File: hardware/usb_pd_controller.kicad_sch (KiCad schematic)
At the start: 85 parts, among them J4 DG142R-5.08-02P-14-00AH, J5 108-0902-001, J6 108-0903-001, Q1 BSS138, Q2 BSS138, Q3 SQJB60EP, Q5 SQJB60EP, U1 AP33772SDKZ-13-FA02, U11 TPS55340PWPR, U12 LM74801-Q1, U13 74LVC1G08, U3 INA226, U5 AOZ1284PI, U6 TL431AIDBZR

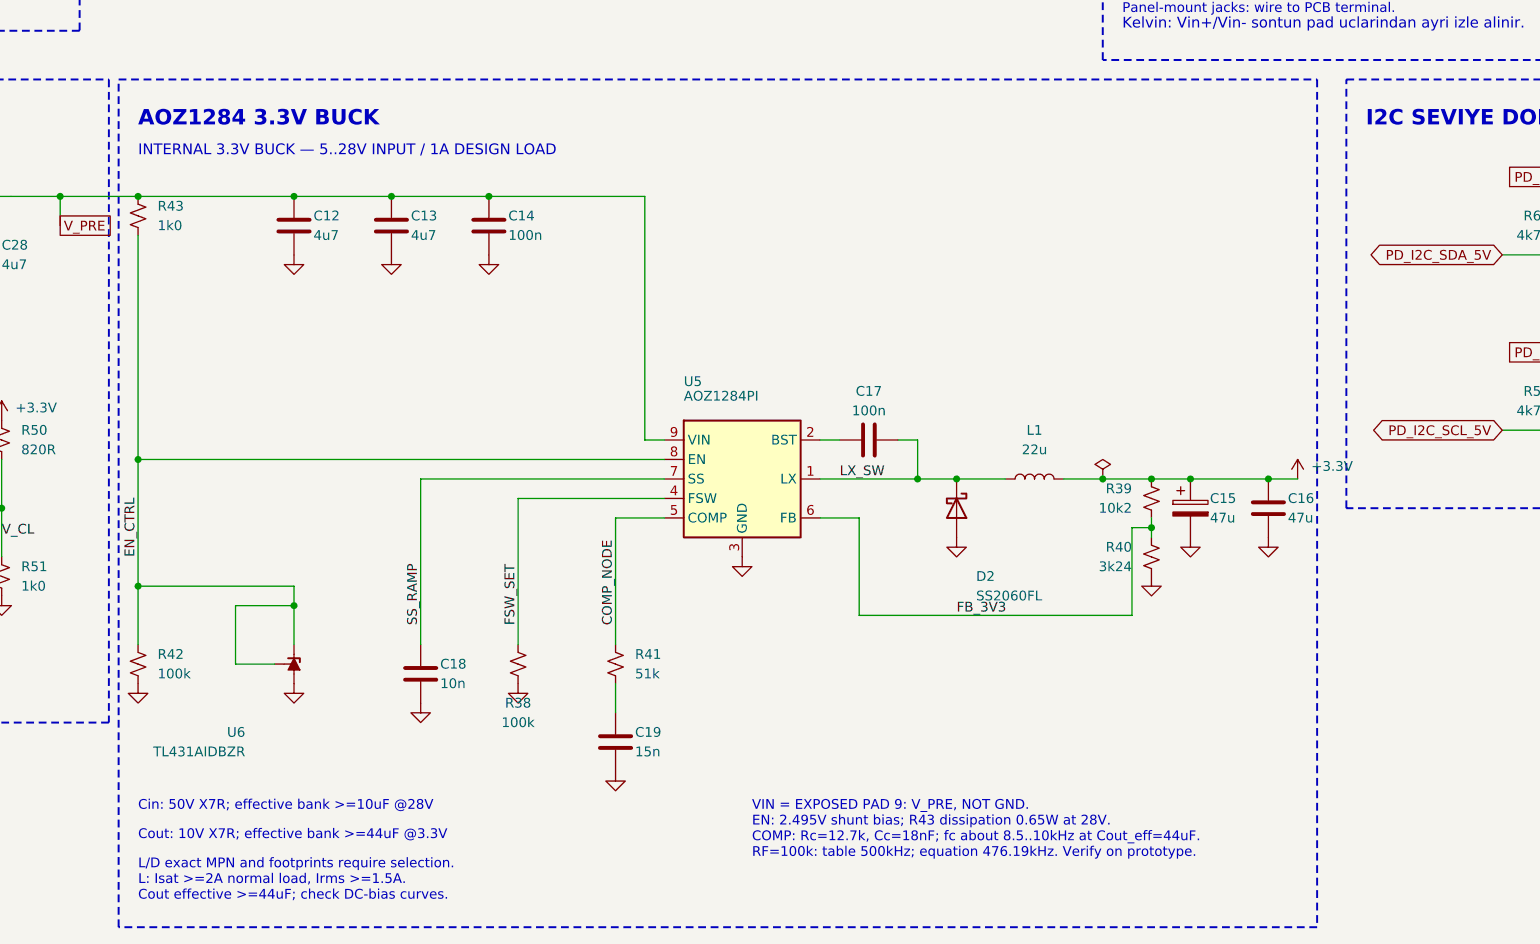
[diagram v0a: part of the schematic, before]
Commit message: hardware: U2'yi ESP32-C6-MINI-1-H4'e geçir, şema notlarını güncelle (TASK-041/004/005)
TASK-041 — U2 ESP32-C6-WROOM-1 -> ESP32-C6-MINI-1-H4 (4 MB flash, -40..105 C,
13,2x16,6 mm). Modül IO10/IO11'i dışarı vermiyor (datasheet v1.5 Tablo 3-1):
- TFT_CS GPIO10 -> GPIO14 (pin 19), TFT_DC GPIO11 -> GPIO7 (pin 16).
- Kullanılan GPIO 0-9 ve 12-23; modülün verdiği kümeyle birebir örtüşüyor,
  boşta GPIO kalmadı. Strapping (4/5/8/9/15) rolleri değişmedi.
- Sembol/footprint KiCad standart kütüphanesinden: RF_Module:ESP32-C6-MINI-1.
- IO8/IO9 MINI-1'de sol kenarda: R37/R15/TP9 ve R10/SW1 U2'nin soluna taşındı,
  iki pull-up tek +3.3V rayını paylaşıyor (#PWR023 kalktı).
- USB seri dirençleri yerinde kaldı, taşıdıkları sinyal yer değiştirdi
  (R2 -> D-, R3 -> D+; USB_DM/USB_DP etiketleri satır değiştirdi).
- Netlist: her net U2 dışındaki üyelerini korudu (yalnız pin numaraları
  değişti), GND'ye modülün tüm toprak pedleri katıldı.

TASK-004 — Eskiyen şema notları: AOZ1284 bloğunda COMP değerleri (Rc=51k,
Cc=15n -> fC ~20 kHz), seçilen L1/D2/Cout parçaları ve "Cout: 10V X7R" hatası
düzeltildi; blok başlığı "V_PRE 5..28V INPUT" oldu. mcu sayfasında çerçeve
dışında kalmış altı eski inceleme sorusu kaldırıldı. Diğer sayfalar tarandı,
güncel.

TASK-005 — USER_İNTERFACE.kicad_sch kaldırıldı (dosya + sayfa sembolü +
.kicad_pro kaydı). İçindeki arayüz sinyal listesi docs/arayuz-sinyalleri.md'ye
güncel pin atamalarıyla taşındı. Sayfa sayısı 6 -> 5.

Doğrulama: ERC 0 hata / 0 uyarı; not/sayfa değişikliklerinde netlist farkı YOK;
okunabilirlik denetiminde yeni bulgu yok (kalan 3 bulgu eskiden beri var).

Ayrıca: TASK-006 footprint listesi güncellendi, TASK-042 açıldı (PCB
güncellemesinden sonra kullanılmayan PCM_Espressif kütüphanesini kaldır),
software/FIRMWARE_GEREKSINIMLERI.md pin haritası yenilendi.

Co-Authored-By: Claude Opus 5 <noreply@anthropic.com>
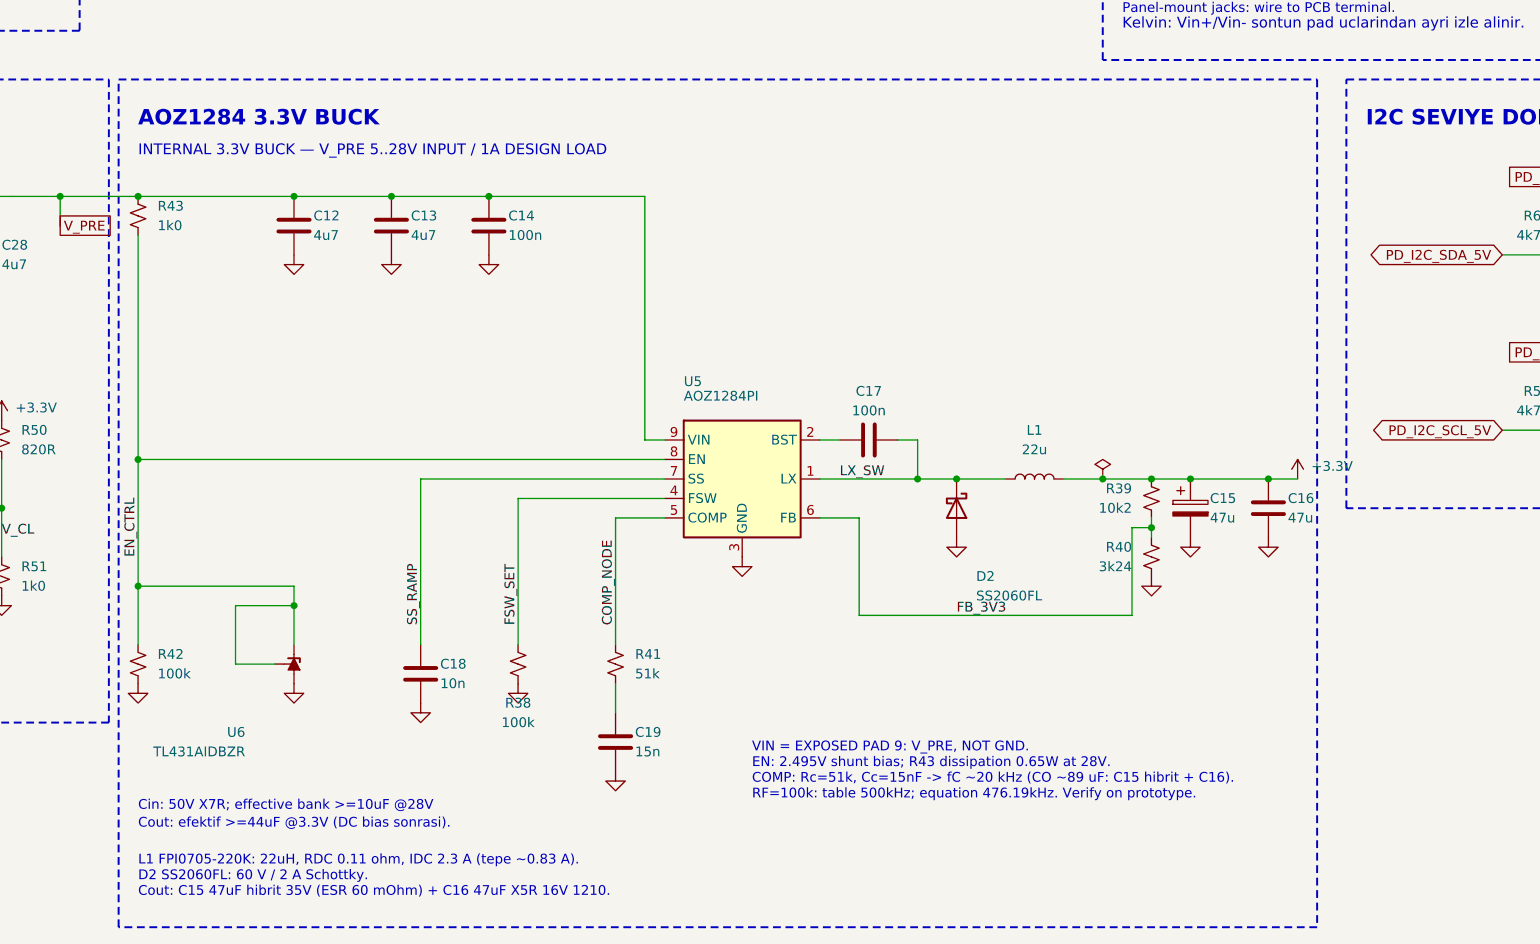
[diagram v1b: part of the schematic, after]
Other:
- note added: "Cout: efektif >=44uF @3.3V (DC bias sonrasi)."
- note added: "INTERNAL 3.3V BUCK — V_PRE 5..28V INPUT / 1A DESIGN LOAD"
- note added: "L1 FPI0705-220K: 22uH, RDC 0.11 ohm, IDC 2.3 A (tepe ~0.83 A). D2 SS2060FL: 60 V / 2 A Schottky. Cout: C15 47uF hibrit 35V (ESR 60 mOhm) + C16 47uF X5R 16V 1210."
- note added: "VIN = EXPOSED PAD 9: V_PRE, NOT GND. EN: 2.495V shunt bias; R43 dissipation 0.65W at 28V. COMP: Rc=51k, Cc=15nF -> fC ~20 kHz (CO ~89 uF: C15 hibrit + C16). RF=100k: table 500kHz; equation 476.19kHz. Verify on prototype."
- note removed: "Cout: 10V X7R; effective bank >=44uF @3.3V"
- note removed: "INTERNAL 3.3V BUCK — 5..28V INPUT / 1A DESIGN LOAD"
- note removed: "L/D exact MPN and footprints require selection. L: Isat >=2A normal load, Irms >=1.5A. Cout effective >=44uF; check DC-bias curves."
- note removed: "VIN = EXPOSED PAD 9: V_PRE, NOT GND. EN: 2.495V shunt bias; R43 dissipation 0.65W at 28V. COMP: Rc=12.7k, Cc=18nF; fc about 8.5..10kHz at Cout_eff=44uF. RF=100k: table 500kHz; equation 476.19kHz. Verify on prototype."
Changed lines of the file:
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@@
 		)
 	)
-	(text "VIN = EXPOSED PAD 9: V_PRE, NOT GND.\nEN: 2.495V shunt bias; R43 dissipation 0.65W at 28V.\nCOMP: Rc=12.7k, Cc=18nF; fc about 8.5..10kHz at Cout_eff=44uF.\nRF=100k: table 500kHz; equation 476.19kHz. Verify on prototype."
-		(exclude_from_sim no)
-		(at 245.11 233.68 0)
-		(effects
-			(font
-				(size 1.27 1.27)
-			)
-			(justify left top)
-		)
-	)
 	(text "V_PRE = 5.02 V  (pass-through > 5.5 V)"
 		(exclude_from_sim no)
@@
 		)
 	)
-	(text "INTERNAL 3.3V BUCK — 5..28V INPUT / 1A DESIGN LOAD"
-		(exclude_from_sim no)
-		(at 165.1 149.86 0)
-		(effects
-			(font
-				(size 1.4 1.4)
-				(color 72 120 180 1)
-			)
-			(justify left bottom)
-		)
-	)
-	(text "L/D exact MPN and footprints require selection.\nL: Isat >=2A normal load, Irms >=1.5A.\nCout effective >=44uF; check DC-bias curves."
-		(exclude_from_sim no)
-		(at 165.1 241.3 0)
-		(effects
-			(font
-				(size 1.27 1.27)
-			)
-			(justify left top)
-		)
-	)
-	(text "Cout: 10V X7R; effective bank >=44uF @3.3V"
-		(exclude_from_sim no)
-		(at 165.1 237.49 0)
-		(effects
-			(font
-				(size 1.27 1.27)
-			)
-			(justify left top)
-		)
-	)
 	(junction
 		(at 266.7 191.77)
@@
 				(color 72 120 180 1)
 			)
+			(justify left bottom)
+		)
+	)
+	(text "VIN = EXPOSED PAD 9: V_PRE, NOT GND.\nEN: 2.495V shunt bias; R43 dissipation 0.65W at 28V.\nCOMP: Rc=51k, Cc=15nF -> fC ~20 kHz (CO ~89 uF: C15 hibrit + C16).\nRF=100k: table 500kHz; equation 476.19kHz. Verify on prototype."
+		(exclude_from_sim no)
+		(at 245.11 233.68 0)
+		(effects
+			(font
+				(size 1.27 1.27)
+				(color 72 120 180 1)
+			)
+			(justify left bottom)
+		)
+	)
+	(text "INTERNAL 3.3V BUCK — V_PRE 5..28V INPUT / 1A DESIGN LOAD"
+		(exclude_from_sim no)
+		(at 165.1 149.86 0)
+		(effects
+			(font
+				(size 1.4 1.4)
+				(color 72 120 180 1)
+			)
+			(justify left bottom)
+		)
+	)
+	(text "Cout: efektif >=44uF @3.3V (DC bias sonrasi)."
+		(exclude_from_sim no)
+		(at 165.1 237.49 0)
+		(effects
+			(font
+				(size 1.27 1.27)
+				(color 72 120 180 1)
+			)
+			(justify left bottom)
+		)
+	)
+	(text "L1 FPI0705-220K: 22uH, RDC 0.11 ohm, IDC 2.3 A (tepe ~0.83 A).\nD2 SS2060FL: 60 V / 2 A Schottky.\nCout: C15 47uF hibrit 35V (ESR 60 mOhm) + C16 47uF X5R 16V 1210."
+		(exclude_from_sim no)
+		(at 165.1 246.38 0)
+		(effects
+			(font
+				(size 1.27 1.27)
+				(color 72 120 180 1)
+			)

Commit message: hardware: R_Small_US, PD_INT bölücüsü, J4 lehim pedi ve Motorobit jaklar (TASK-043/044/045)
- Tüm dirençler Device:R -> Device:R_Small_US (21 sembol); netlist değişmedi.
- R8 12k / R9 20k -> R8 10k + R64 2k0 / R9 10k + R65 10k (oran 0.625,
  en kötü 2.73..3.34 V). BOM'dan 12k ve 20k kalktı.
- J4 DG142R klemens -> SolderWire-1.5sqmm 1x02 lehim pedi; J5/J6 ->
  Motorobit 4 mm banana (KOM.KNN.06.000021/22). Netlist değişmedi.
- Beklenen netlist farkı: PD_INT_3V3 = R64.2, R9.1, TP8.1, U2.26;
  Net-(R64-Pad1) = R8.2, R64.1; Net-(R65-Pad1) = R9.2, R65.1;
  GND'de R9.2 -> R65.2. ERC 0 hata / 0 uyarı.
- Takip: TASK-046/047 (jak numunesi), TASK-006/008'e AC eklendi.

Co-Authored-By: Claude Opus 5.5 <noreply@anthropic.com>
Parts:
- added R64: 2k0, Resistor_SMD:R_0402_1005Metric, symbol Device:R_Small_US
- added R65: 10k, Resistor_SMD:R_0402_1005Metric, symbol Device:R_Small_US
- J4: value DG142R-5.08-02P-14-00AH -> SolderWire-1.5sqmm; footprint DG142R-5.08-02P-14-00AH:DG142R-5.08-02P-14-00AH -> Connector_Wire:SolderWire-1.5sqmm_1x02_P7.8mm_D1.7mm_OD3.9mm; symbol DG142R-5.08-02P-14-00AH:DG142R-5.08-02P-14-00AH -> Connector_Generic:Conn_01x02; DesignNote 2 kutuplu 5.08 mm klemens; cikis terminali. -> Maks. cikis 3 A (CIKIS_AKIMI_3A_KARARI_20260922). Kablo 1.5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; MPN DG142R-5.08-02P-14-00AH -> N/A (PCB pedi); Manufacturer DEGSON -> N/A
- J5: value 108-0902-001 -> Banana_4mm_Red; DesignNote PANEL MOUNT; J4'e kablo ile gider, kart uzerinde yalniz mek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 -> Footprint yalniz panel kesimi (Cinch 108-090x double-D); Mo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; MPN 108-0902-001 -> KOM.KNN.06.000021; Manufacturer Cinch Johnson -> Motorobit; SelectionNote Özdisan (21.09.2026): İndekste yok. 21.09 ikinci kontrol: b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 -> Motorobit KOM.KNN.06.000021; stok 100+ (23.09.2026). Akim/g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
- J6: value 108-0903-001 -> Banana_4mm_Black; DesignNote PANEL MOUNT; J4'e kablo ile gider, kart uzerinde yalniz mek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 -> Footprint yalniz panel kesimi (Cinch 108-090x double-D); Mo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; MPN 108-0903-001 -> KOM.KNN.06.000022; Manufacturer Cinch Johnson -> Motorobit; SelectionNote Özdisan (21.09.2026): İndekste yok. 21.09 ikinci kontrol: b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 -> Motorobit KOM.KNN.06.000022; stok 100+ (23.09.2026). Akim/g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
- R11, R12, R13, R14, R21, R27, R4, R5, R6, R7, RShunt1: symbol Device:R -> Device:R_Small_US
- R8: value 12k -> 10k; symbol Device:R -> Device:R_Small_US; Composition Thick Film -> Thin Film; DesignNote TBD -> PD_INT 5V->3V3 bolucu: R8+R64 = 10k+2k0 (12k), R9+R65 = 2x1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; MPN CRCW040212K0FKED -> TC0250B1002TCC; Manufacturer Vishay -> Royalohm; SelectionNote Özdisan 519356; stok 6761 (21.09.2026); Uygun. -> Özdisan 569744; stok 4220 (21.09.2026); Uygun. Özdisan'da 0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; TempCoefficient +/-100ppm/C -> +/-50ppm/C; Tolerance +/-1% -> +/-0.1%; VoltageRating 50V -> 25V
- R9: value 20k -> 10k; symbol Device:R -> Device:R_Small_US; DesignNote TBD -> PD_INT 5V->3V3 bolucu: R8+R64 = 10k+2k0 (12k), R9+R65 = 2x1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; MPN TC0250B2002TCC -> TC0250B1002TCC; SelectionNote Özdisan 570296; stok 3225 (21.09.2026); Uygun. 0402 20k %1 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 -> Özdisan 569744; stok 4220 (21.09.2026); Uygun. Özdisan'da 0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
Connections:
- net GND: now also R65.2; no longer R9.2
- net PD_INT_3V3: now also R64.2; no longer R8.2
- new net: R65.1, R9.2
- new net: R64.1, R8.2
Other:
- moved on the sheet: J4
